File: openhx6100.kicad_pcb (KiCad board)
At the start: 2 copper layers, 36 x 52 mm, 41 parts, among them J1 USB_C_Receptacle_PowerOnly_6P, Q1 DMG1012T, Q3 DMG1012T, Q5 DMG2301L, Q6 DMG2301L, Q7 DMG1012T, Q8 DMG1012T, U1 74HC14, U2 TLC555xD

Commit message: layout: finish layout
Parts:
- H1, H2, H3, H4: footprint MountingHole:MountingHole_3.2mm_M3_DIN965_Pad -> MountingHole:MountingHole_2.2mm_M2_DIN965_Pad
- Q1, Q3, Q7, Q8: footprint Package_TO_SOT_SMD:SOT-523 -> Gigahawk:SOT-523
- RV1: footprint Potentiometer_SMD:Potentiometer_Bourns_TC33X_Vertical -> Gigahawk:Potentiometer_Bourns_TC33X_Vertical
- TP10, TP3, TP4, TP5, TP6, TP7, TP8, TP9: footprint TestPoint:TestPoint_Keystone_5010-5014_Multipurpose -> Gigahawk:TestPoint_Keystone_5000-5004_Miniature

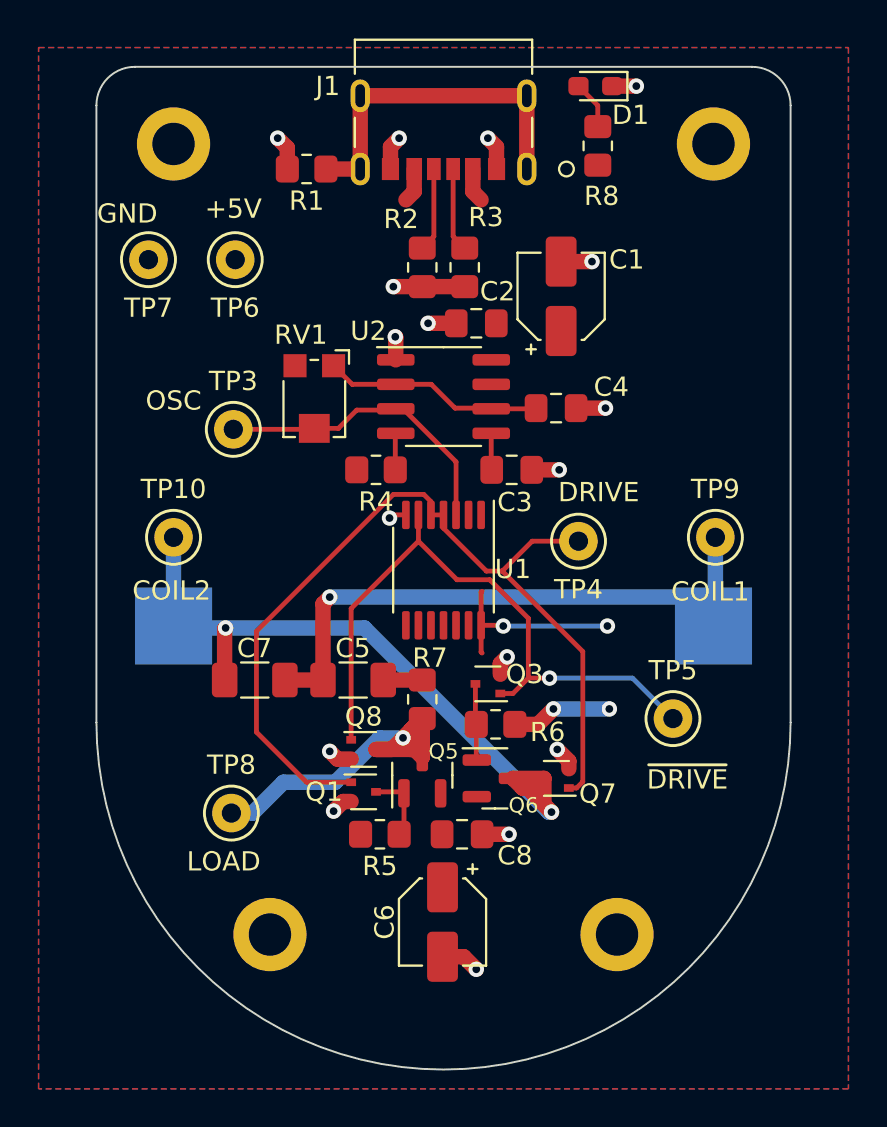
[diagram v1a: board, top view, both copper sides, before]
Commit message: bom: fill out bom
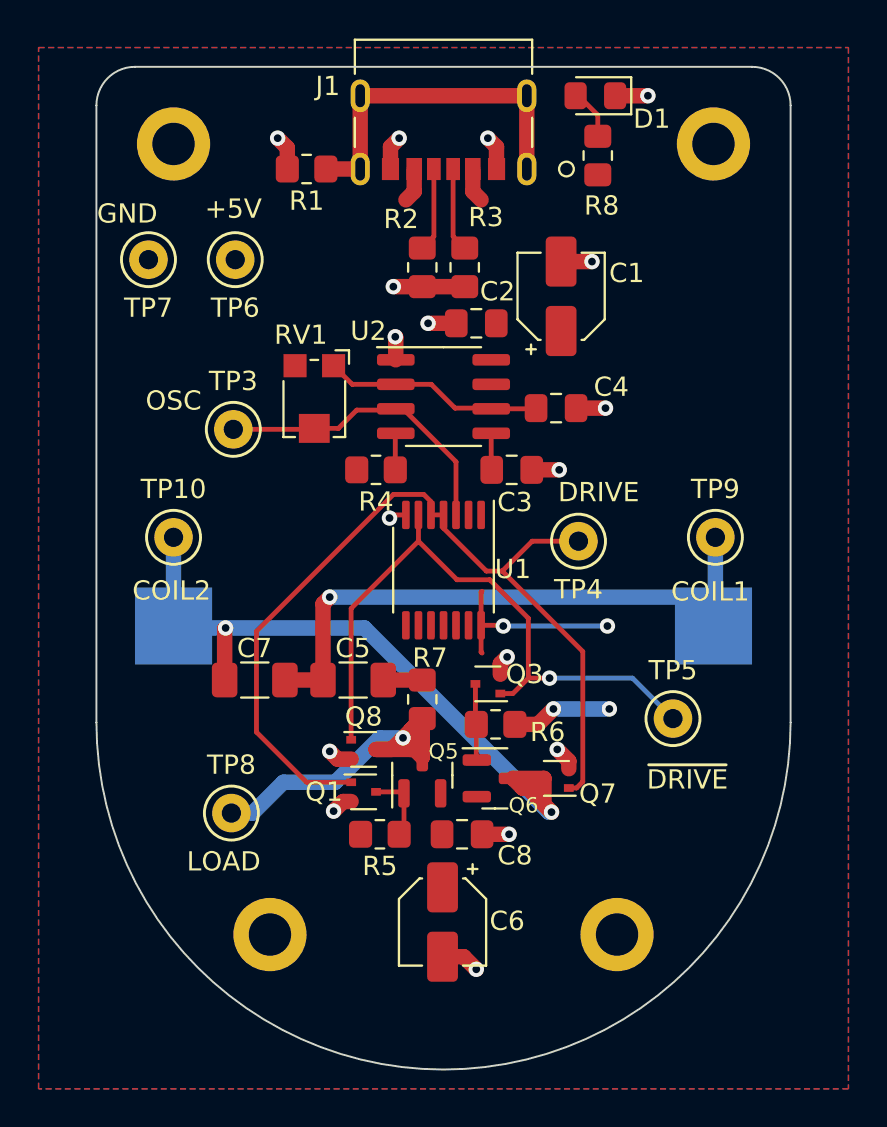
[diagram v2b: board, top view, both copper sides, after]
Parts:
- C1, C6: value 1u -> 10u; footprint Capacitor_SMD:CP_Elec_4x4.5 -> Capacitor_SMD:CP_Elec_4x5.4
- D1: footprint LED_SMD:LED_0603_1608Metric_Pad1.05x0.95mm_HandSolder -> LED_SMD:LED_0805_2012Metric_Pad1.15x1.40mm_HandSolder
- moved D1 0.50 mm to (7.88, 1.50)
- moved R8 0.50 mm to (8.00, 4.60)
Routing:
- net GND: track 26.6 -> 27.2 mm

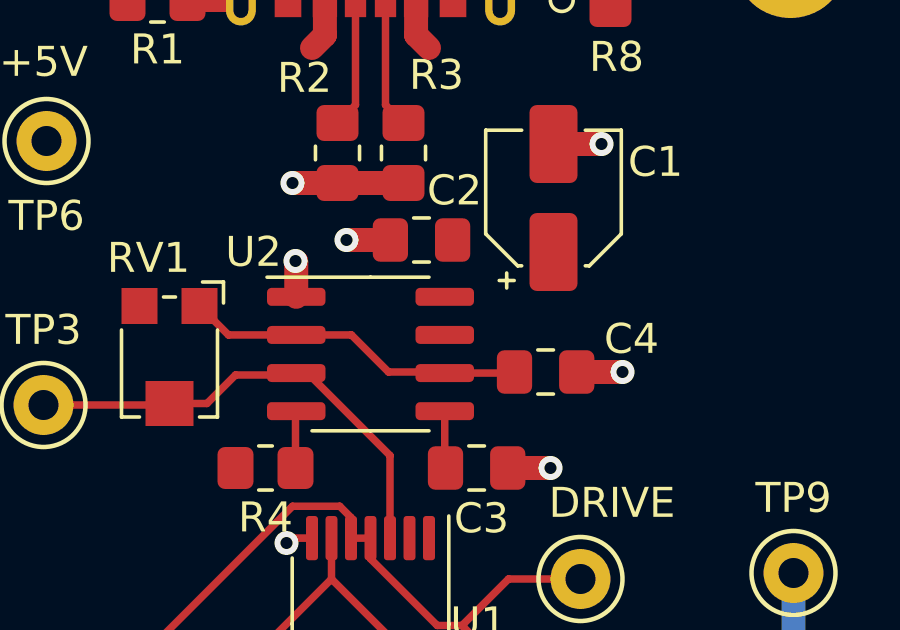
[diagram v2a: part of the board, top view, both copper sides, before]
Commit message: feature: add revision info
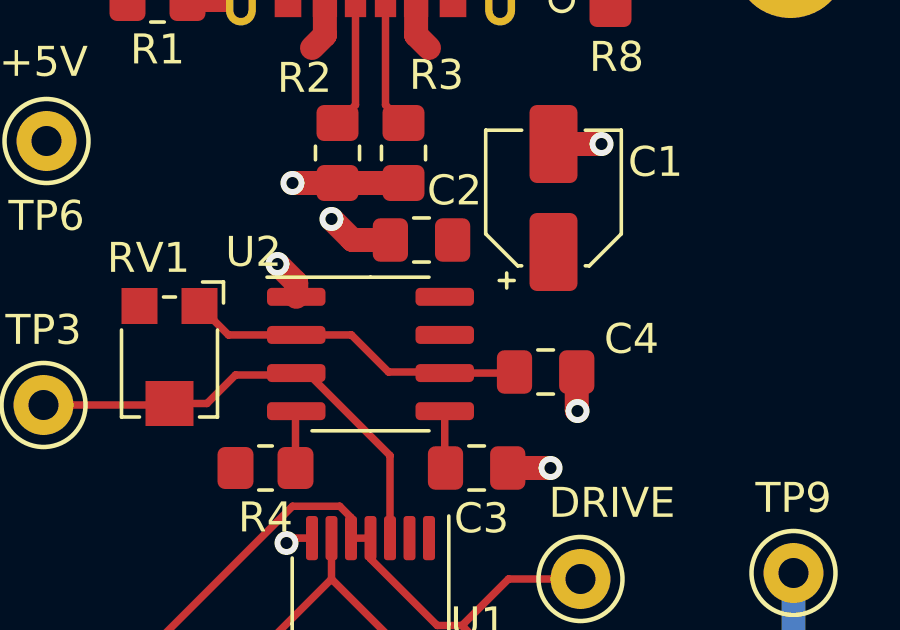
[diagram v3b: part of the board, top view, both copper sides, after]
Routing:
- net GND: track 27.2 -> 27.9 mm
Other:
- board text added: "Gigahawk/openhx6100 Revision: ${TAG} (${HASH}) Date: ${DATE}"
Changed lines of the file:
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@@
     )
   )
+  (property "DATE" "YYYY-MM-DD HH:MM:SS")
+  (property "HASH" "HASH")
+  (property "TAG" "TAG")
   (net 0 "")
   (net 1 "+5V")
@@
     (effects (font (size 1 1) (thickness 0.15)) (justify bottom))
   )
+  (gr_text "Gigahawk/openhx6100\nRevision: ${TAG} (${HASH})\nDate: ${DATE}\n" (at 14.7 18.4) (layer "B.Mask")
+    (effects (font (size 1 1) (thickness 0.15)) (justify left bottom mirror))
+  )
   (segment (start 1.95 28.9625) (end 3.0625 28.9625) (width 0.254) (layer "F.Cu") (net 1))
   (segment (start 3.7 34.1) (end 4.9 34.1) (width 0.8) (layer "F.Cu") (net 1))
@@
   (segment (start 2.945 31.5) (end 2.945 30.955) (width 0.8) (layer "F.Cu") (net 2))
   (segment (start -8.1 5.3) (end -8.1 4.2) (width 0.8) (layer "F.Cu") (net 2))
-  (segment (start 6.875 17.7) (end 8.4 17.7) (width 0.8) (layer "F.Cu") (net 2))
   (segment (start -8.1 4.2) (end -8.6 3.7) (width 0.8) (layer "F.Cu") (net 2))
   (segment (start -2.75 4.15) (end -2.3 3.7) (width 0.8) (layer "F.Cu") (net 2))
   (segment (start -1.1 11.4) (end 1.1 11.4) (width 0.8) (layer "F.Cu") (net 2))
   (segment (start -5.2 38.1) (end -5.7 38.6) (width 0.8) (layer "F.Cu") (net 2))
+  (segment (start -2.475 14.725) (end -2.475 15.195) (width 0.8) (layer "F.Cu") (net 2))
   (segment (start -1.1 11.4) (end -2.6 11.4) (width 0.8) (layer "F.Cu") (net 2))
   (segment (start 6.1 10.1) (end 7.7 10.1) (width 0.8) (layer "F.Cu") (net 2))
-  (segment (start -2.475 15.195) (end -2.475 14.025) (width 0.8) (layer "F.Cu") (net 2))
   (segment (start 1.05 46.15) (end 1.7 46.8) (width 0.8) (layer "F.Cu") (net 2))
+  (segment (start -0.6 13.3) (end -1.3 12.6) (width 0.8) (layer "F.Cu") (net 2))
+  (segment (start 0.6625 13.3) (end -0.6 13.3) (width 0.8) (layer "F.Cu") (net 2))
   (segment (start 2.75 4.15) (end 2.3 3.7) (width 0.8) (layer "F.Cu") (net 2))
-  (segment (start -2.475 14.025) (end -2.5 14) (width 0.8) (layer "F.Cu") (net 2))
   (segment (start 4.575 20.9) (end 6 20.9) (width 0.8) (layer "F.Cu") (net 2))
   (segment (start 6.5 36) (end 5.9 35.4) (width 0.8) (layer "F.Cu") (net 2))
-  (segment (start 0.6625 13.3) (end -0.8 13.3) (width 0.8) (layer "F.Cu") (net 2))
   (segment (start -2.6375 23.2375) (end -2.8 23.4) (width 0.254) (layer "F.Cu") (net 2))
   (segment (start -4.79 38.1) (end -5.2 38.1) (width 0.8) (layer "F.Cu") (net 2))
@@
   (segment (start 6.5 36.4) (end 6.5 36) (width 0.8) (layer "F.Cu") (net 2))
   (segment (start -1.95 23.2375) (end -2.6375 23.2375) (width 0.254) (layer "F.Cu") (net 2))
+  (segment (start -3.1 14.1) (end -2.475 14.725) (width 0.8) (layer "F.Cu") (net 2))
   (segment (start 2.75 5.3) (end 2.75 4.15) (width 0.8) (layer "F.Cu") (net 2))
   (segment (start 8.75 1.5) (end 10.6 1.5) (width 0.8) (layer "F.Cu") (net 2))
+  (segment (start 6.875 18.975) (end 6.9 19) (width 0.8) (layer "F.Cu") (net 2))
+  (segment (start 6.875 17.7) (end 6.875 18.975) (width 0.8) (layer "F.Cu") (net 2))
   (segment (start -2.75 5.3) (end -2.75 4.15) (width 0.8) (layer "F.Cu") (net 2))
   (via (at 2.3 3.7) (size 0.8) (drill 0.4) (layers "F.Cu" "B.Cu") (net 2))
@@
   (via (at 10.6 1.5) (size 0.8) (drill 0.4) (layers "F.Cu" "B.Cu") (net 2))
   (via (at -2.8 23.4) (size 0.8) (drill 0.4) (layers "F.Cu" "B.Cu") (net 2))
-  (via (at -0.8 13.3) (size 0.8) (drill 0.4) (layers "F.Cu" "B.Cu") (net 2))
+  (via (at -1.3 12.6) (size 0.8) (drill 0.4) (layers "F.Cu" "B.Cu") (net 2))
   (via (at -2.6 11.4) (size 0.8) (drill 0.4) (layers "F.Cu" "B.Cu") (net 2))
-  (via (at 8.4 17.7) (size 0.8) (drill 0.4) (layers "F.Cu" "B.Cu") (net 2))
+  (via (at 6.9 19) (size 0.8) (drill 0.4) (layers "F.Cu" "B.Cu") (net 2))
   (via (at 1.7 46.8) (size 0.8) (drill 0.4) (layers "F.Cu" "B.Cu") (net 2))
   (via (at 3.3 30.6) (size 0.8) (drill 0.4) (layers "F.Cu" "B.Cu") (net 2))
@@
   (via (at 7.7 10.1) (size 0.8) (drill 0.4) (layers "F.Cu" "B.Cu") (net 2))
   (via (at 6 20.9) (size 0.8) (drill 0.4) (layers "F.Cu" "B.Cu") (net 2))
-  (via (at -2.5 14) (size 0.8) (drill 0.4) (layers "F.Cu" "B.Cu") (net 2))
+  (via (at -3.1 14.1) (size 0.8) (drill 0.4) (layers "F.Cu" "B.Cu") (net 2))
   (via (at -8.6 3.7) (size 0.8) (drill 0.4) (layers "F.Cu" "B.Cu") (net 2))
   (segment (start 2.475 19.005) (end 2.475 20.875) (width 0.25) (layer "F.Cu") (net 3))
